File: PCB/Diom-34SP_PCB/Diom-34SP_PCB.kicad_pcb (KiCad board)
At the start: 2 copper layers, 133.5 x 101.1 mm, 30 parts, among them J1 Conn_01x02_Male, SW1 SHOU_HAN_MSK12C02-HB, U1 nice_nano

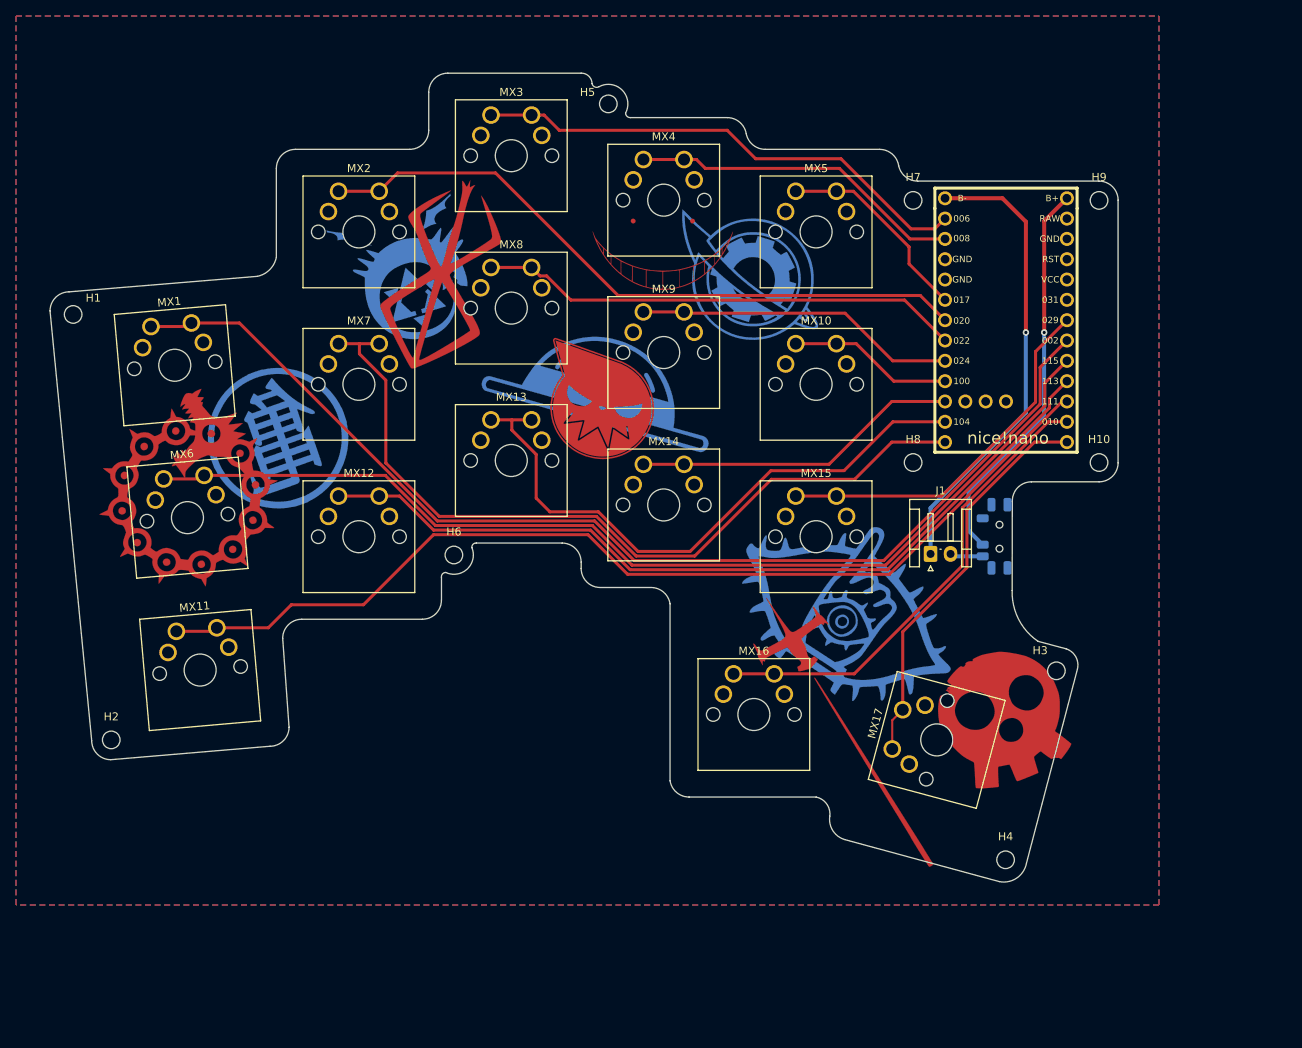
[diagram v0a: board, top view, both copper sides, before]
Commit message: Massive Changes
-New Switch
-New Outline
-More Mounting Holes
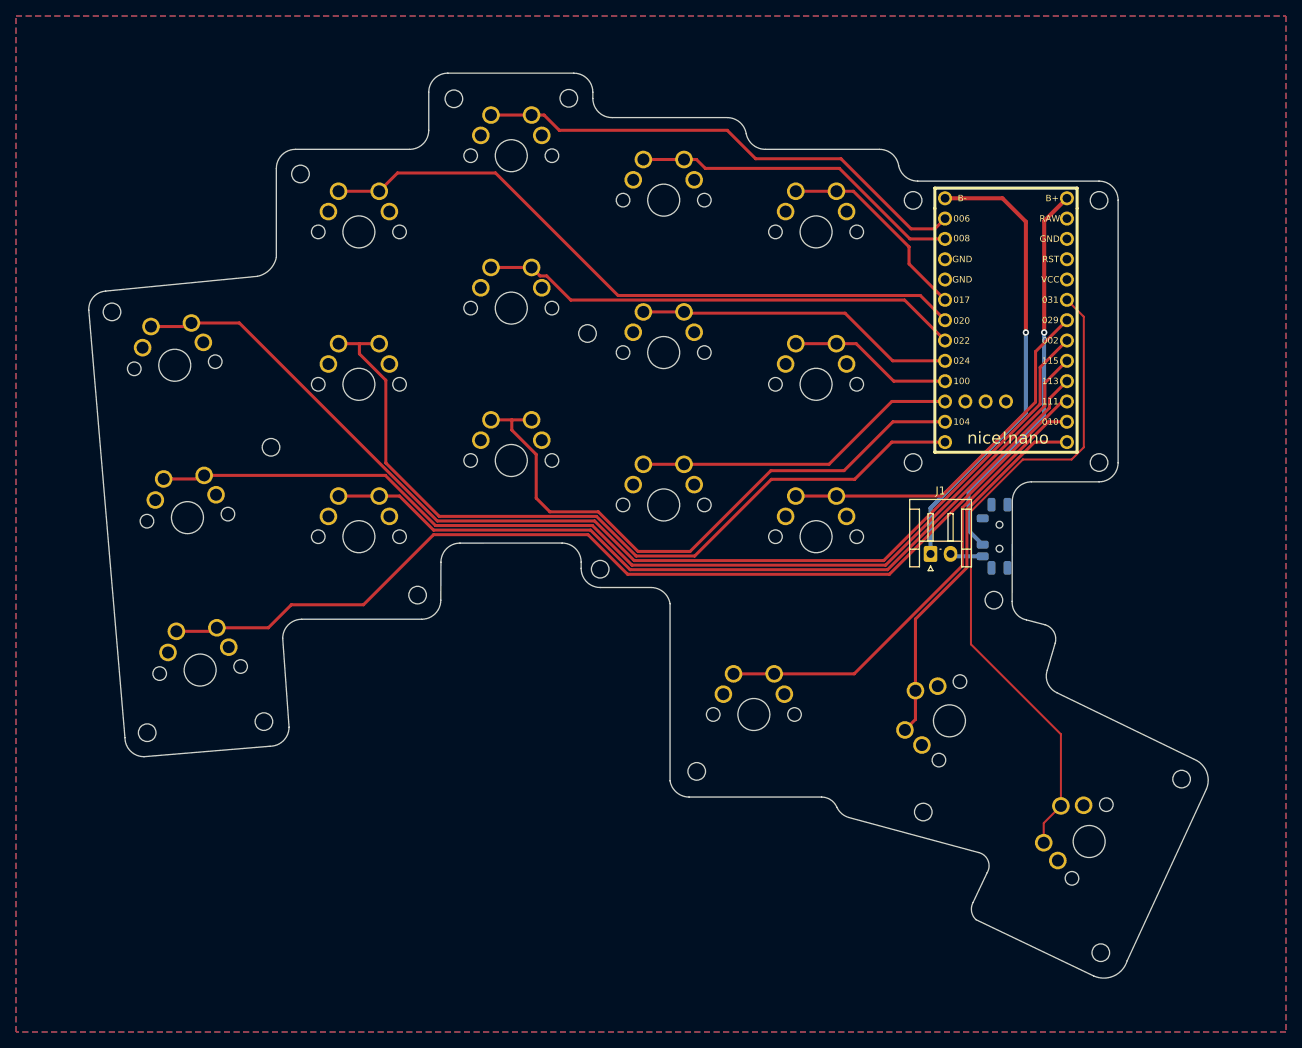
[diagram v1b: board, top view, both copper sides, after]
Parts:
- added H11: MountingHole, MountingHole:MountingHole_2.2mm_M2_DIN965, F.Cu at (185.7, 96.8)
- added H12: MountingHole, MountingHole:MountingHole_2.2mm_M2_DIN965, F.Cu at (176.9, 123.3)
- added H13: MountingHole, MountingHole:MountingHole_2.2mm_M2_DIN965, F.Cu at (134.9, 63.5)
- added H14: MountingHole, MountingHole:MountingHole_2.2mm_M2_DIN965, F.Cu at (148.6, 118.2)
- added H15: MountingHole, MountingHole:MountingHole_2.2mm_M2_DIN965, F.Cu at (118.2, 34.2)
- added H16: MountingHole, MountingHole:MountingHole_2.2mm_M2_DIN965, F.Cu at (136.5, 93.0)
- added H17: MountingHole, MountingHole:MountingHole_2.2mm_M2_DIN965, F.Cu at (95.4, 77.7)
- added H18: MountingHole, MountingHole:MountingHole_2.2mm_M2_DIN965, F.Cu at (99.1, 43.6)
- added H19: MountingHole, MountingHole:MountingHole_2.2mm_M2_DIN965, F.Cu at (94.5, 112.0)
- added MX18: MX-NoLED, mx-switches-doubleSided:CherryMX-1.5U-doubleSided-Vertical-noSilk, F.Cu at (197.6, 127.0)
- MX1, MX10, MX11, MX12, MX13, MX14, MX15, MX16, MX2, MX3, MX4, MX5, MX6, MX7, MX8, MX9: footprint mx-switches-doubleSided:CherryMX-1U-doubleSided -> mx-switches-doubleSided:CherryMX-1U-doubleSided-noSilk
- MX17: footprint mx-switches-doubleSided:CherryMX-1.5U-doubleSided-Vertical -> mx-switches-doubleSided:CherryMX-1.5U-doubleSided-Vertical-noSilk
- moved H3 20.7 mm to (209.2, 119.2)
- moved H4 16.6 mm to (199.1, 140.9)
- moved H6 6.76 mm to (113.7, 96.2)
- moved H5 4.99 mm to (132.6, 34.1)
- moved H1 4.87 mm to (75.5, 60.8)
- moved H2 4.58 mm to (79.9, 113.4)
- moved MX17 2.86 mm to (180.2, 111.9)
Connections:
- U1 pad 20: unconnected-(U1-Pad20) -> MX18
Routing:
- net MX18: track 0.00 -> 83.7 mm
- net MX17: track 49.8 -> 46.7 mm
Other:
- board size 133.5 x 101.1 mm -> 139.9 x 113.1 mm
